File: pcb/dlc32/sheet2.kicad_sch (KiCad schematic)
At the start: 27 parts, among them IC2 74HCT04, J10 VALVE/CHILLER SSR PWR, J11 Conn_01x02, J14 Conn_02x05_Odd_Even, J15 Conn_01x05, J16 Conn_01x03, J4 CHILLER SWITCH, J5 CHILLER SSR, J6 AIR VALVE, J9 AIMING LASER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

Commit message: Use resistor array.
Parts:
- C6, C7, C8: footprint Capacitor_SMD:CP_Elec_10x10 -> PCM_Capacitor_SMD_AKL:CP_Elec_10x10
- D6: footprint LED_THT:LED_D5.0mm_Horizontal_O1.27mm_Z3.0mm -> PCM_LED_THT_AKL:LED_D5.0mm_Horizontal_O1.27mm_Z3.0mm
- R11, R12: footprint Resistor_SMD:R_0603_1608Metric -> PCM_Resistor_SMD_AKL:R_0603_1608Metric
- R15: renamed from R17; footprint Resistor_SMD:R_0603_1608Metric -> PCM_Resistor_SMD_AKL:R_0603_1608Metric
- R16: renamed from R18; footprint Resistor_SMD:R_0603_1608Metric -> PCM_Resistor_SMD_AKL:R_0603_1608Metric
- R17: renamed from R19; footprint Resistor_SMD:R_0603_1608Metric -> PCM_Resistor_SMD_AKL:R_0603_1608Metric
- R2: renamed from R20; footprint Resistor_SMD:R_0603_1608Metric -> PCM_Resistor_SMD_AKL:R_0603_1608Metric
- R3: renamed from R15; footprint Resistor_SMD:R_0603_1608Metric -> PCM_Resistor_SMD_AKL:R_0603_1608Metric
- R4: renamed from R16; footprint Resistor_SMD:R_0603_1608Metric -> PCM_Resistor_SMD_AKL:R_0603_1608Metric
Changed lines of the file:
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@@
 			)
 		)
-		(property "Footprint" "Capacitor_SMD:CP_Elec_10x10"
+		(property "Footprint" "PCM_Capacitor_SMD_AKL:CP_Elec_10x10"
 			(at 53.0352 177.8 0)
 			(effects
@@
 			)
 		)
-		(property "Footprint" "Resistor_SMD:R_0603_1608Metric"
+		(property "Footprint" "PCM_Resistor_SMD_AKL:R_0603_1608Metric"
 			(at 48.26 107.442 90)
 			(effects
@@
 			)
 		)
-		(property "Footprint" "Resistor_SMD:R_0603_1608Metric"
+		(property "Footprint" "PCM_Resistor_SMD_AKL:R_0603_1608Metric"
 			(at 38.862 114.3 90)
 			(effects
@@
 		(on_board yes)
 		(dnp no)
-		(property "Reference" "R18"
+		(property "Reference" "R16"
 			(at 143.51 45.5422 90)
 			(effects
@@
 			)
 		)
-		(property "Footprint" "Resistor_SMD:R_0603_1608Metric"
+		(property "Footprint" "PCM_Resistor_SMD_AKL:R_0603_1608Metric"
 			(at 143.51 49.022 90)
 			(effects
@@
 			(project "dlc32"
 				(path "/fc0b2ef6-7d8e-4322-8468-8fac0c3c3d07/00000000-0000-0000-0000-000058f3b713"
-					(reference "R18")
+					(reference "R16")
 					(unit 1)
 				)
@@
 		(dnp no)
 		(fields_autoplaced yes)
-		(property "Reference" "R20"
+		(property "Reference" "R2"
 			(at 82.55 105.4099 0)
 			(effects
@@
 			)
 		)
-		(property "Footprint" "Resistor_SMD:R_0603_1608Metric"
+		(property "Footprint" "PCM_Resistor_SMD_AKL:R_0603_1608Metric"
 			(at 78.232 106.68 90)
 			(effects
@@
 			(project ""
 				(path "/fc0b2ef6-7d8e-4322-8468-8fac0c3c3d07/00000000-0000-0000-0000-000058f3b713"
-					(reference "R20")
+					(reference "R2")
 					(unit 1)
 				)
@@
 		(on_board yes)
 		(dnp no)
-		(property "Reference" "R19"
+		(property "Reference" "R17"
 			(at 185.42 45.5422 90)
 			(effects
@@
 			)
 		)
-		(property "Footprint" "Resistor_SMD:R_0603_1608Metric"
+		(property "Footprint" "PCM_Resistor_SMD_AKL:R_0603_1608Metric"
 			(at 185.42 49.022 90)
 			(effects
@@
 			(project "dlc32"
 				(path "/fc0b2ef6-7d8e-4322-8468-8fac0c3c3d07/00000000-0000-0000-0000-000058f3b713"
-					(reference "R19")
+					(reference "R17")
 					(unit 1)
 				)
@@
 		(on_board yes)
 		(dnp no)
-		(property "Reference" "R16"
+		(property "Reference" "R4"
 			(at 115.57 45.5422 90)
 			(effects
@@
 			)
 		)
-		(property "Footprint" "Resistor_SMD:R_0603_1608Metric"
+		(property "Footprint" "PCM_Resistor_SMD_AKL:R_0603_1608Metric"
 			(at 115.57 49.022 90)
 			(effects
@@
 			(project "dlc32"
 				(path "/fc0b2ef6-7d8e-4322-8468-8fac0c3c3d07/00000000-0000-0000-0000-000058f3b713"
-					(reference "R16")
+					(reference "R4")
 					(unit 1)
 				)
@@
 		(on_board yes)
 		(dnp no)
-		(property "Reference" "R15"
+		(property "Reference" "R3"
 			(at 77.978 57.2516 0)
 			(effects
@@
 			)
 		)
-		(property "Footprint" "Resistor_SMD:R_0603_1608Metric"
+		(property "Footprint" "PCM_Resistor_SMD_AKL:R_0603_1608Metric"
 			(at 74.422 58.42 90)
 			(effects
@@
 			(project "dlc32"
 				(path "/fc0b2ef6-7d8e-4322-8468-8fac0c3c3d07/00000000-0000-0000-0000-000058f3b713"
-					(reference "R15")
+					(reference "R3")
 					(unit 1)
 				)
@@
 			)
 		)
-		(property "Footprint" "LED_THT:LED_D5.0mm_Horizontal_O1.27mm_Z3.0mm"
+		(property "Footprint" "PCM_LED_THT_AKL:LED_D5.0mm_Horizontal_O1.27mm_Z3.0mm"
 			(at 80.01 116.84 0)
 			(effects
@@
 		(on_board yes)
 		(dnp no)
-		(property "Reference" "R17"
+		(property "Reference" "R15"
 			(at 131.318 57.2516 0)
 			(effects
@@
 			)
 		)
-		(property "Footprint" "Resistor_SMD:R_0603_1608Metric"
+		(property "Footprint" "PCM_Resistor_SMD_AKL:R_0603_1608Metric"
 			(at 127.762 58.42 90)
 			(effects
@@
 			(project "dlc32"
 				(path "/fc0b2ef6-7d8e-4322-8468-8fac0c3c3d07/00000000-0000-0000-0000-000058f3b713"
-					(reference "R17")
+					(reference "R15")
 					(unit 1)
 				)
@@
 			)
 		)
-		(property "Footprint" "Capacitor_SMD:CP_Elec_10x10"
+		(property "Footprint" "PCM_Capacitor_SMD_AKL:CP_Elec_10x10"
 			(at 135.5852 173.99 0)
 			(effects
@@
 			)
 		)
-		(property "Footprint" "Capacitor_SMD:CP_Elec_10x10"
+		(property "Footprint" "PCM_Capacitor_SMD_AKL:CP_Elec_10x10"
 			(at 139.3952 62.23 0)
 			(effects

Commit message: Add optional +5V power, route.
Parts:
- added J17: Conn_01x02, Connector_PinHeader_2.54mm:PinHeader_1x02_P2.54mm_Vertical, symbol Connector_Generic:Conn_01x02
- added J18: Conn_01x02, Connector_JST:JST_XH_B2B-XH-A_1x02_P2.50mm_Vertical, symbol Connector_Generic:Conn_01x02
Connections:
- net +5V: now also J17.1 (Pin_1), J18.1 (Pin_1); no longer J14.1 (Pin_1)
- net GND: now also J18.2 (Pin_2)
- new net: J14.1 (Pin_1), J17.2 (Pin_2)
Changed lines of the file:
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@@
 	)
 	(junction
+		(at 149.86 80.01)
+		(diameter 0)
+		(color 0 0 0 0)
+	)
+	(junction
 		(at 62.23 120.65)
 		(diameter 1.016)
@@
 	)
 	(junction
+		(at 153.67 82.55)
+		(diameter 0)
+		(color 0 0 0 0)
+	)
+	(junction
 		(at 198.12 63.5)
 		(diameter 1.016)
@@
 	(wire
 		(pts
+			(xy 149.86 91.44) (xy 149.86 80.01)
+		)
+		(stroke
+			(width 0)
+			(type default)
+		)
+	)
+	(wire
+		(pts
 			(xy 210.82 22.86) (xy 210.82 26.67)
 		)
@@
 	(wire
 		(pts
+			(xy 153.67 82.55) (xy 153.67 85.09)
+		)
+		(stroke
+			(width 0)
+			(type default)
+		)
+	)
+	(wire
+		(pts
 			(xy 40.64 168.91) (xy 52.07 168.91)
 		)
@@
 	(wire
 		(pts
+			(xy 149.86 80.01) (xy 149.86 76.2)
+		)
+		(stroke
+			(width 0)
+			(type default)
+		)
+	)
+	(wire
+		(pts
 			(xy 62.23 120.65) (xy 80.01 120.65)
 		)
@@
 	(wire
 		(pts
+			(xy 153.67 82.55) (xy 171.45 82.55)
+		)
+		(stroke
+			(width 0)
+			(type default)
+		)
+	)
+	(wire
+		(pts
 			(xy 147.32 50.8) (xy 148.59 50.8)
 		)
@@
 	(wire
 		(pts
+			(xy 147.32 91.44) (xy 149.86 91.44)
+		)
+		(stroke
+			(width 0)
+			(type default)
+		)
+	)
+	(wire
+		(pts
+			(xy 171.45 82.55) (xy 171.45 97.79)
+		)
+		(stroke
+			(width 0)
+			(type default)
+		)
+	)
+	(wire
+		(pts
 			(xy 134.62 173.99) (xy 134.62 176.53)
 		)
@@
 	(wire
 		(pts
+			(xy 147.32 93.98) (xy 147.32 97.79)
+		)
+		(stroke
+			(width 0)
+			(type default)
+		)
+	)
+	(wire
+		(pts
 			(xy 76.2 63.5) (xy 129.54 63.5)
 		)
@@
 	(wire
 		(pts
-			(xy 68.58 96.52) (xy 68.58 102.87)
+			(xy 147.32 80.01) (xy 149.86 80.01)
 		)
 		(stroke
@@
 	(wire
 		(pts
-			(xy 146.05 100.33) (xy 153.67 100.33)
+			(xy 68.58 96.52) (xy 68.58 102.87)
 		)
 		(stroke
@@
 	(wire
 		(pts
-			(xy 62.23 99.06) (xy 62.23 102.87)
+			(xy 146.05 100.33) (xy 153.67 100.33)
 		)
 		(stroke
 			(width 0)
-			(type solid)
+			(type default)
 		)
 	)
 	(wire
 		(pts
-			(xy 138.43 63.5) (xy 198.12 63.5)
+			(xy 62.23 99.06) (xy 62.23 102.87)
 		)
 		(stroke
@@
 	(wire
 		(pts
-			(xy 96.52 101.6) (xy 93.98 101.6)
+			(xy 138.43 63.5) (xy 198.12 63.5)
 		)
 		(stroke
 			(width 0)
-			(type default)
+			(type solid)
 		)
 	)
 	(wire
 		(pts
-			(xy 171.45 95.25) (xy 171.45 97.79)
+			(xy 96.52 101.6) (xy 93.98 101.6)
 		)
 		(stroke
@@
 	(wire
 		(pts
-			(xy 147.32 88.9) (xy 147.32 97.79)
+			(xy 147.32 82.55) (xy 153.67 82.55)
 		)
 		(stroke
@@
 	)
 	(symbol
+		(lib_id "Connector_Generic:Conn_01x02")
+		(at 142.24 80.01 0)
+		(mirror y)
+		(unit 1)
+		(exclude_from_sim no)
+		(in_bom yes)
+		(on_board yes)
+		(dnp no)
+		(property "Reference" "J18"
+			(at 137.922 81.28 0)
+			(effects
+				(font
+					(size 1.27 1.27)
+				)
+			)
+		)
+		(property "Value" "Conn_01x02"
+			(at 142.24 76.2 0)
+			(effects
+				(font
+					(size 1.27 1.27)
+				)
+				(hide yes)
+			)
+		)
+		(property "Footprint" "Connector_JST:JST_XH_B2B-XH-A_1x02_P2.50mm_Vertical"
+			(at 142.24 80.01 0)
+			(effects
+				(font
+					(size 1.27 1.27)
+				)
+				(hide yes)
+			)
+		)
+		(property "Datasheet" "~"
+			(at 142.24 80.01 0)
+			(effects
+				(font
+					(size 1.27 1.27)
+				)
+				(hide yes)
+			)
+		)
+		(property "Description" "Generic connector, single row, 01x02, script generated (kicad-library-utils/schlib/autogen/connector/)"
+			(at 142.24 80.01 0)
+			(effects
+				(font
+					(size 1.27 1.27)
+				)
+				(hide yes)
+			)
+		)
+		(pin "1"
+		)
+		(pin "2"
+		)
+		(instances
+			(project ""
+				(path "/fc0b2ef6-7d8e-4322-8468-8fac0c3c3d07/00000000-0000-0000-0000-000058f3b713"
+					(reference "J18")
+					(unit 1)
+				)
+			)
+		)
+	)
+	(symbol
 		(lib_id "Connector_Generic:Conn_01x03")
 		(at 204.47 132.08 0)
@@
 	(symbol
 		(lib_id "power:GND")
-		(at 171.45 95.25 180)
+		(at 153.67 85.09 0)
 		(unit 1)
 		(exclude_from_sim no)
@@
 		(dnp no)
 		(property "Reference" "#PWR020"
-			(at 171.45 88.9 0)
+			(at 153.67 91.44 0)
 			(effects
 				(font
@@
 		)
 		(property "Value" "GND"
-			(at 171.196 91.186 0)
+			(at 153.924 89.154 0)
 			(effects
 				(font
@@
 		)
 		(property "Footprint" ""
-			(at 171.45 95.25 0)
+			(at 153.67 85.09 0)
 			(effects
 				(font
@@
 		)
 		(property "Datasheet" ""
-			(at 171.45 95.25 0)
+			(at 153.67 85.09 0)
 			(effects
 				(font
@@
 		)
 		(property "Description" "Power symbol creates a global label with name \"GND\" , ground"
-			(at 171.45 95.25 0)
+			(at 153.67 85.09 0)
 			(effects
 				(font
@@
 	(symbol
 		(lib_id "power:+5V")
-		(at 147.32 88.9 0)
+		(at 149.86 76.2 0)
 		(unit 1)
 		(exclude_from_sim no)
@@
 		(fields_autoplaced yes)
 		(property "Reference" "#PWR017"
-			(at 147.32 92.71 0)
+			(at 149.86 80.01 0)
 			(effects
 				(font
@@
 		)
 		(property "Value" "+5V"
-			(at 147.32 83.82 0)
+			(at 149.86 71.12 0)
 			(effects
 				(font
@@
 		)
 		(property "Footprint" ""
-			(at 147.32 88.9 0)
+			(at 149.86 76.2 0)
 			(effects
 				(font
@@
 		)
 		(property "Datasheet" ""
-			(at 147.32 88.9 0)
+			(at 149.86 76.2 0)
 			(effects
 				(font
@@
 		)
 		(property "Description" "Power symbol creates a global label with name \"+5V\""
-			(at 147.32 88.9 0)
+			(at 149.86 76.2 0)
 			(effects
 				(font
@@
 					(unit 1)
 				)
+			)
+		)
+	)
+	(symbol
+		(lib_id "Connector_Generic:Conn_01x02")
+		(at 142.24 91.44 0)
+		(mirror y)
+		(unit 1)
+		(exclude_from_sim no)
+		(in_bom yes)
+		(on_board yes)
+		(dnp no)
+		(property "Reference" "J17"
+			(at 138.176 92.456 0)
+			(effects
+				(font
+					(size 1.27 1.27)
+				)
+			)
+		)
+		(property "Value" "Conn_01x02"
+			(at 142.24 87.63 0)
+			(effects
+				(font
+					(size 1.27 1.27)
+				)
+				(hide yes)
+			)
+		)
+		(property "Footprint" "Connector_PinHeader_2.54mm:PinHeader_1x02_P2.54mm_Vertical"
+			(at 142.24 91.44 0)
+			(effects
+				(font
+					(size 1.27 1.27)
+				)
+				(hide yes)
+			)
+		)
+		(property "Datasheet" "~"
+			(at 142.24 91.44 0)
+			(effects
+				(font
+					(size 1.27 1.27)
+				)
+				(hide yes)
+			)
+		)
+		(property "Description" "Generic connector, single row, 01x02, script generated (kicad-library-utils/schlib/autogen/connector/)"
+			(at 142.24 91.44 0)
+			(effects
+				(font
+					(size 1.27 1.27)
+				)
+				(hide yes)
+			)
+		)
+		(pin "1"
+		)
+		(pin "2"
+		)
+		(instances
+			(project ""
+				(path "/fc0b2ef6-7d8e-4322-8468-8fac0c3c3d07/00000000-0000-0000-0000-000058f3b713"
+					(reference "J17")
+					(unit 1)
+				)

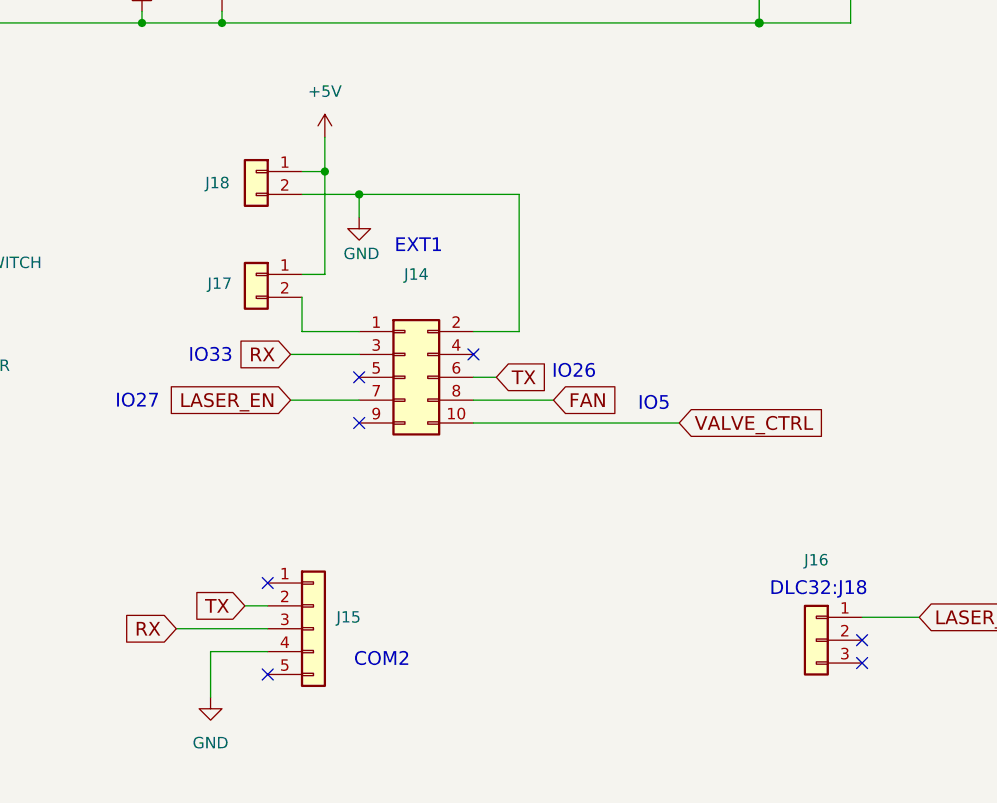
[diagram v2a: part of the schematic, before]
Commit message: Fix footprint for R1.
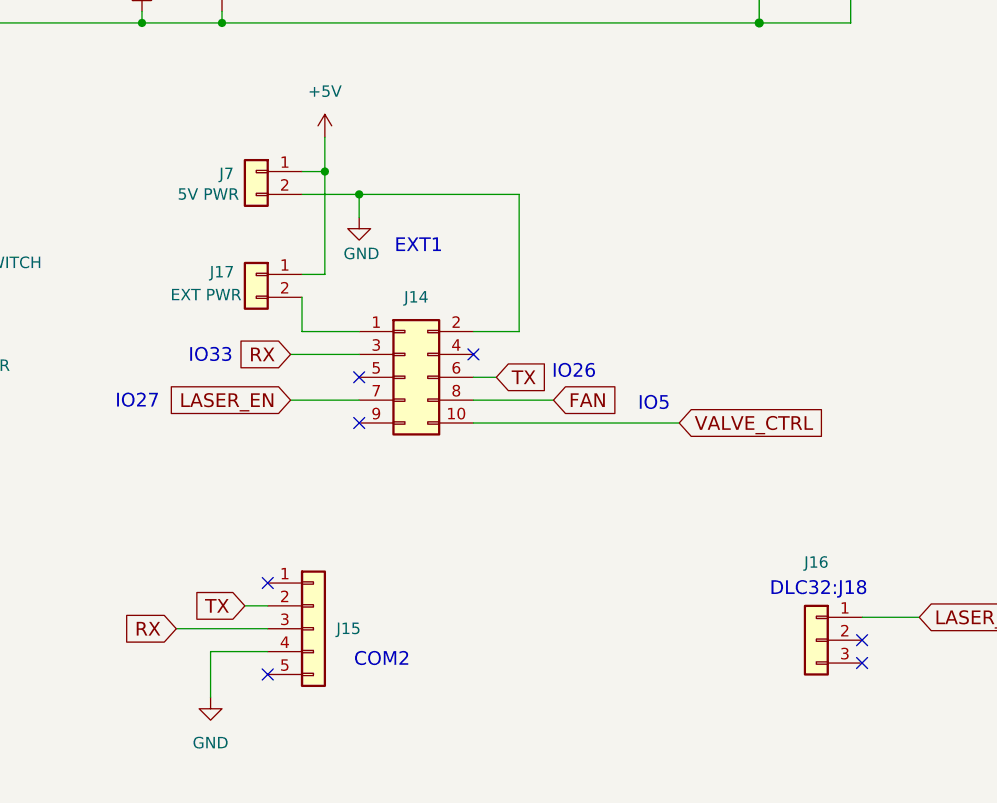
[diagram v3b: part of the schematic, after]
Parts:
- J11: value Conn_01x02 -> EXHAUST
- J14: value Conn_02x05_Odd_Even -> EXT1
- J15: value Conn_01x05 -> COM2
- J16: value Conn_01x03 -> DLC32:J18
- J17: value Conn_01x02 -> EXT PWR
- J7: renamed from J18; value Conn_01x02 -> 5V PWR
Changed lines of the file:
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@@
 		(on_board yes)
 		(dnp no)
-		(property "Reference" "J18"
-			(at 137.922 81.28 0)
-			(effects
-				(font
-					(size 1.27 1.27)
-				)
-			)
-		)
-		(property "Value" "Conn_01x02"
-			(at 142.24 76.2 0)
-			(effects
-				(font
-					(size 1.27 1.27)
-				)
-				(hide yes)
+		(property "Reference" "J7"
+			(at 138.938 80.264 0)
+			(effects
+				(font
+					(size 1.27 1.27)
+				)
+			)
+		)
+		(property "Value" "5V PWR"
+			(at 136.906 82.55 0)
+			(effects
+				(font
+					(size 1.27 1.27)
+				)
 			)
 		)
@@
 			(project ""
 				(path "/fc0b2ef6-7d8e-4322-8468-8fac0c3c3d07/00000000-0000-0000-0000-000058f3b713"
-					(reference "J18")
+					(reference "J7")
 					(unit 1)
 				)
@@
 		(on_board yes)
 		(dnp no)
-		(fields_autoplaced yes)
 		(property "Reference" "J16"
-			(at 204.47 123.19 0)
-			(effects
-				(font
-					(size 1.27 1.27)
-				)
-			)
-		)
-		(property "Value" "Conn_01x03"
+			(at 204.47 123.444 0)
+			(effects
+				(font
+					(size 1.27 1.27)
+				)
+			)
+		)
+		(property "Value" "DLC32:J18"
 			(at 204.47 125.73 0)
 			(effects
@@
 		(fields_autoplaced yes)
 		(property "Reference" "J15"
-			(at 151.13 129.5399 0)
+			(at 151.13 130.8099 0)
 			(effects
 				(font
@@
 			)
 		)
-		(property "Value" "Conn_01x05"
+		(property "Value" "COM2"
 			(at 151.13 132.0799 0)
 			(effects
@@
 		(fields_autoplaced yes)
 		(property "Reference" "J14"
-			(at 160.02 91.44 0)
-			(effects
-				(font
-					(size 1.27 1.27)
-				)
-			)
-		)
-		(property "Value" "Conn_02x05_Odd_Even"
+			(at 160.02 93.98 0)
+			(effects
+				(font
+					(size 1.27 1.27)
+				)
+			)
+		)
+		(property "Value" "EXT1"
 			(at 160.02 93.98 0)
 			(effects
@@
 			)
 		)
-		(property "Value" "Conn_01x02"
+		(property "Value" "EXHAUST"
 			(at 219.202 53.3146 0)
 			(effects
@@
 		(dnp no)
 		(property "Reference" "J17"
-			(at 138.176 92.456 0)
-			(effects
-				(font
-					(size 1.27 1.27)
-				)
-			)
-		)
-		(property "Value" "Conn_01x02"
-			(at 142.24 87.63 0)
-			(effects
-				(font
-					(size 1.27 1.27)
-				)
-				(hide yes)
-			)
-		)
+			(at 138.43 91.186 0)
+			(effects
+				(font
+					(size 1.27 1.27)
+				)
+			)
+		)
+		(property "Value" "EXT PWR"
+			(at 136.652 93.726 0)
+			(effects
+				(font
+					(size 1.27 1.27)
+				)
+			)
+		)

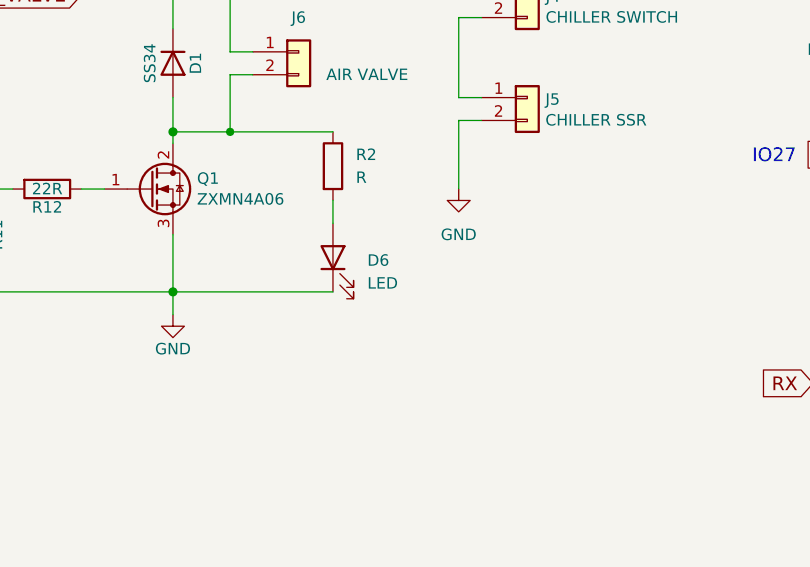
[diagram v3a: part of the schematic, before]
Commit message: Make pretty.
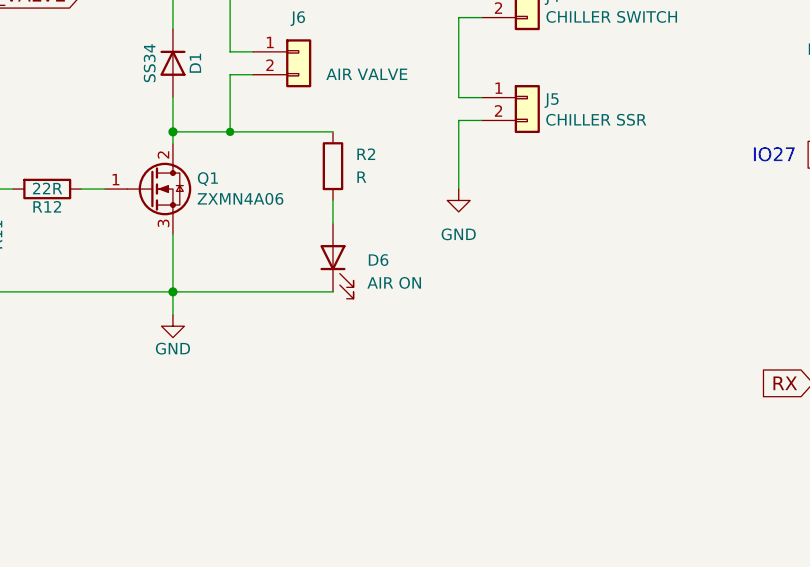
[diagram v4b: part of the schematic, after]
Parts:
- D6: value LED -> AIR ON
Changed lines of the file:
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@@
 			)
 		)
-		(property "Value" "LED"
+		(property "Value" "AIR ON"
 			(at 83.82 119.6974 90)
 			(effects
